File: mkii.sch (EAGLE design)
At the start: 52 parts, among them IC1 ATMEGA32U2, Q1 16MHz, U1 GTL2003, U2 TS1117, U3 PRTR5V0U2AX, X1 MINI-USB-32005-301

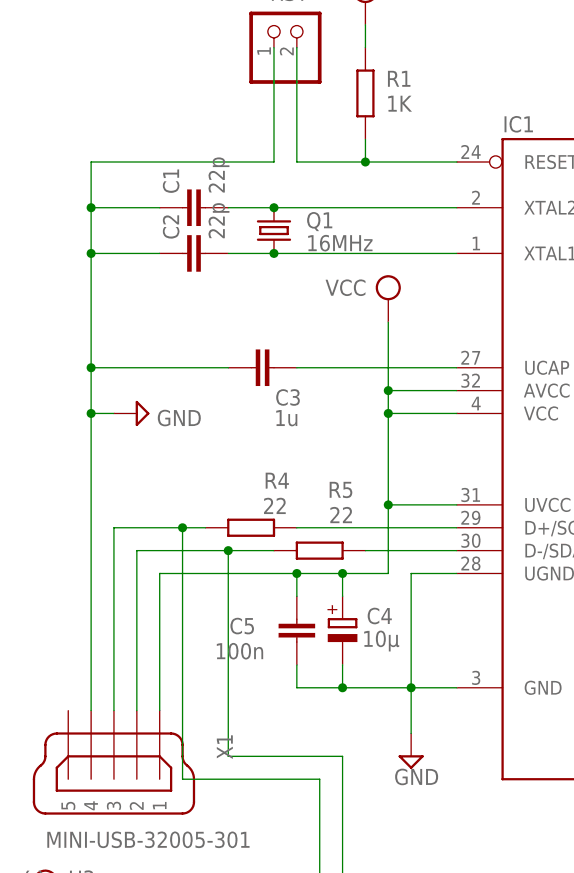
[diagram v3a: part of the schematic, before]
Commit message: pin4 on usb is id, pin5 is gnd. upstream idiots.
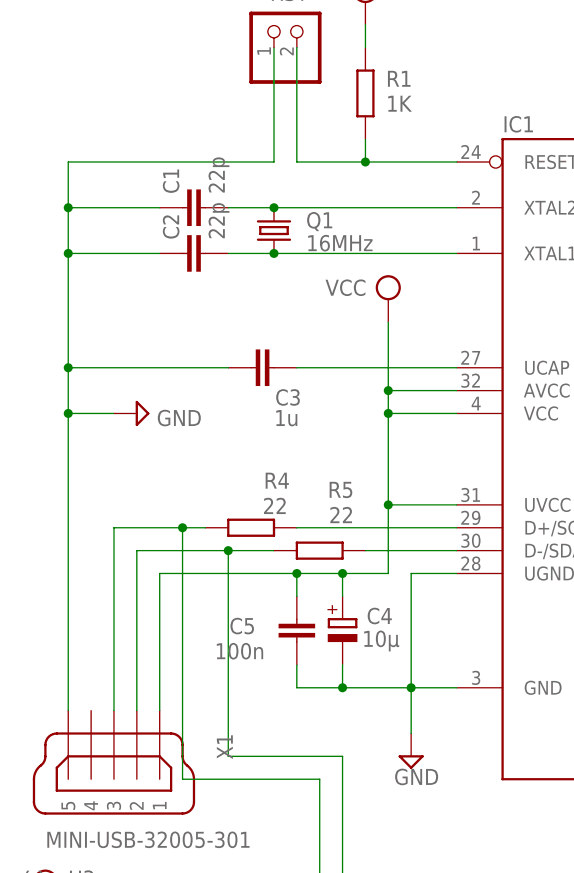
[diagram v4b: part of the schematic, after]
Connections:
- net GND: now also X1.5; no longer X1.4
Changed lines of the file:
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@@
 <net name="GND" class="1">
 <segment>
-<wire x1="20.32" y1="116.84" x2="12.7" y2="116.84" width="0.1524" layer="91"/>
-<wire x1="12.7" y1="116.84" x2="12.7" y2="111.76" width="0.1524" layer="91"/>
-<wire x1="20.32" y1="111.76" x2="12.7" y2="111.76" width="0.1524" layer="91"/>
-<wire x1="27.94" y1="99.06" x2="12.7" y2="99.06" width="0.1524" layer="91"/>
-<wire x1="12.7" y1="99.06" x2="12.7" y2="93.98" width="0.1524" layer="91"/>
-<wire x1="33.02" y1="121.92" x2="12.7" y2="121.92" width="0.1524" layer="91"/>
-<wire x1="12.7" y1="121.92" x2="12.7" y2="116.84" width="0.1524" layer="91"/>
-<wire x1="12.7" y1="60.96" x2="12.7" y2="93.98" width="0.1524" layer="91"/>
-<wire x1="12.7" y1="93.98" x2="15.24" y2="93.98" width="0.1524" layer="91"/>
-<wire x1="12.7" y1="111.76" x2="12.7" y2="99.06" width="0.1524" layer="91"/>
+<wire x1="20.32" y1="116.84" x2="10.16" y2="116.84" width="0.1524" layer="91"/>
+<wire x1="10.16" y1="116.84" x2="10.16" y2="111.76" width="0.1524" layer="91"/>
+<wire x1="20.32" y1="111.76" x2="10.16" y2="111.76" width="0.1524" layer="91"/>
+<wire x1="27.94" y1="99.06" x2="10.16" y2="99.06" width="0.1524" layer="91"/>
+<wire x1="10.16" y1="99.06" x2="10.16" y2="93.98" width="0.1524" layer="91"/>
+<wire x1="33.02" y1="121.92" x2="10.16" y2="121.92" width="0.1524" layer="91"/>
+<wire x1="10.16" y1="121.92" x2="10.16" y2="116.84" width="0.1524" layer="91"/>
+<wire x1="10.16" y1="93.98" x2="15.24" y2="93.98" width="0.1524" layer="91"/>
+<wire x1="10.16" y1="111.76" x2="10.16" y2="99.06" width="0.1524" layer="91"/>
 <wire x1="33.02" y1="121.92" x2="33.02" y2="134.62" width="0.1524" layer="91"/>
-<junction x="12.7" y="111.76"/>
-<junction x="12.7" y="116.84"/>
-<junction x="12.7" y="93.98"/>
-<junction x="12.7" y="99.06"/>
+<junction x="10.16" y="111.76"/>
+<junction x="10.16" y="116.84"/>
+<junction x="10.16" y="99.06"/>
 <pinref part="C1" gate="G$1" pin="1"/>
 <pinref part="C2" gate="G$1" pin="1"/>
@@
 <pinref part="RST" gate="A" pin="1"/>
 <pinref part="C3" gate="G$1" pin="1"/>
-<pinref part="X1" gate="G$1" pin="4"/>
+<pinref part="X1" gate="G$1" pin="5"/>
+<wire x1="10.16" y1="93.98" x2="10.16" y2="60.96" width="0.1524" layer="91"/>
+<junction x="10.16" y="93.98"/>
 </segment>
 <segment>

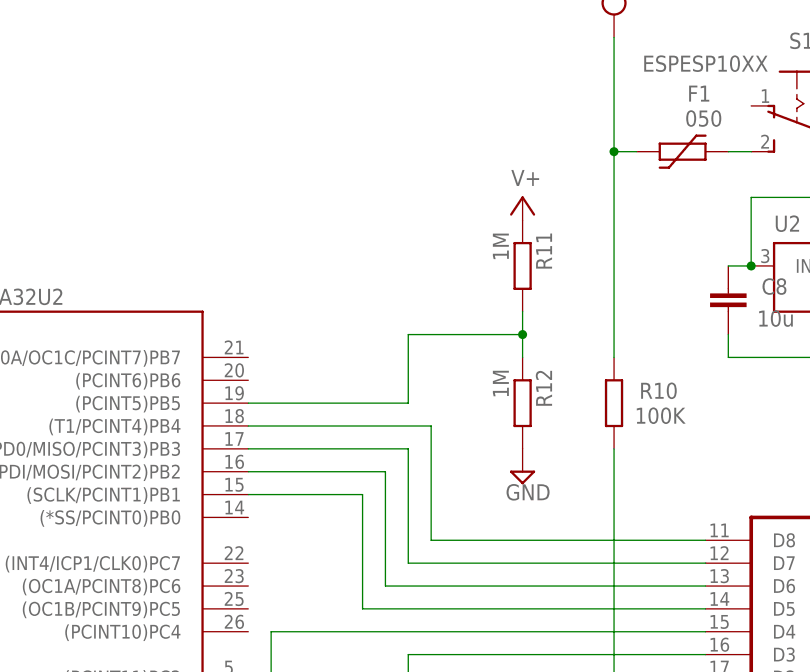
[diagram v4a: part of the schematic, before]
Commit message: remote circuit on pb5
can't remember my thoughts – without ADC there is no vbus
detection.
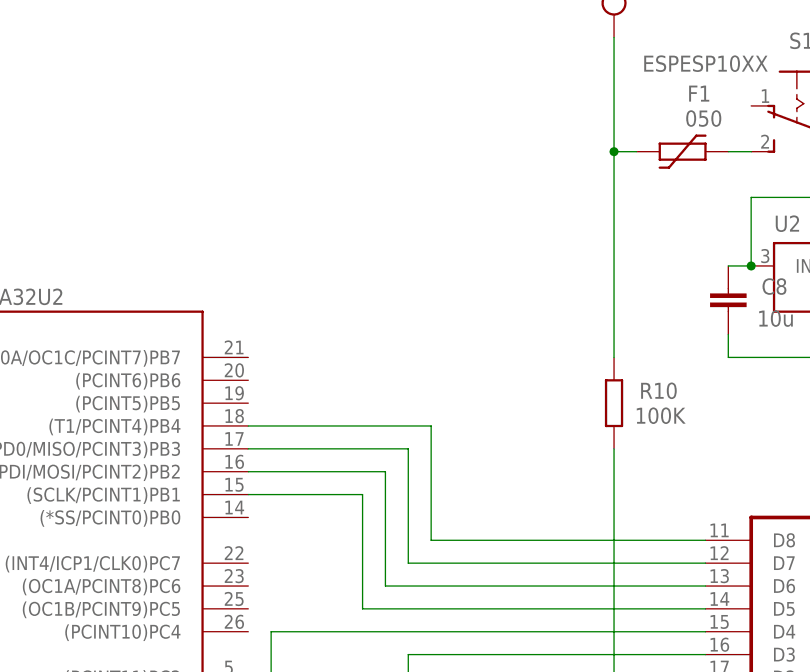
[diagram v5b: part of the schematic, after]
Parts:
- removed R11, R12: 1M, rcl:R-EU_R0603
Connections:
- removed net N$5: IC1.(PCINT5)PB5, R11.2, R12.1
- net GND: no longer R12.2
- net V+: no longer R11.1
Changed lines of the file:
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@@
 <part name="SV3" library="con-ml" deviceset="ML6" device="" value="TPI"/>
 <part name="FRAME1" library="frames" deviceset="A4L-LOC" device=""/>
-<part name="R11" library="rcl" deviceset="R-EU_" device="R0603" value="1M"/>
-<part name="R12" library="rcl" deviceset="R-EU_" device="R0603" value="1M"/>
-<part name="SUPPLY16" library="supply2" deviceset="GND" device=""/>
-<part name="SUPPLY17" library="supply2" deviceset="V+" device=""/>
 <part name="U$1" library="creative-commons" deviceset="CC" device="-TPLACE-HALF"/>
 <part name="U$2" library="creative-commons" deviceset="BY" device="-TPLACE-HS"/>
@@
 <instance part="SV3" gate="1" x="223.52" y="55.88" rot="R180"/>
 <instance part="FRAME1" gate="G$1" x="0" y="0"/>
-<instance part="R11" gate="G$1" x="134.62" y="129.54" rot="R270"/>
-<instance part="R12" gate="G$1" x="134.62" y="114.3" rot="R270"/>
-<instance part="SUPPLY16" gate="GND" x="134.62" y="106.68" smashed="yes">
-<attribute name="VALUE" x="132.715" y="103.505" size="1.778" layer="96"/>
-</instance>
-<instance part="SUPPLY17" gate="1" x="134.62" y="137.16" smashed="yes">
-<attribute name="VALUE" x="133.35" y="138.43" size="1.778" layer="96"/>
-</instance>
 <instance part="U$1" gate="G$1" x="215.9" y="20.32"/>
 <instance part="U$2" gate="G$1" x="220.98" y="20.32"/>
@@
 </segment>
 <segment>
-<pinref part="R12" gate="G$1" pin="2"/>
-<pinref part="SUPPLY16" gate="GND" pin="GND"/>
-</segment>
-<segment>
 <pinref part="U3" gate="G$1" pin="GND"/>
 <pinref part="SUPPLY18" gate="GND" pin="GND"/>
@@
 <wire x1="238.76" y1="86.36" x2="231.14" y2="86.36" width="0.1524" layer="91"/>
 </segment>
-<segment>
-<pinref part="R11" gate="G$1" pin="1"/>
-<pinref part="SUPPLY17" gate="1" pin="V+"/>
-</segment>
 </net>
 <net name="N$16" class="0">
@@
 </segment>
 </net>
-<net name="N$5" class="0">
-<segment>
-<pinref part="IC1" gate="AT90USB162" pin="(PCINT5)PB5"/>
-<wire x1="104.14" y1="114.3" x2="121.92" y2="114.3" width="0.1524" layer="91"/>
-<wire x1="121.92" y1="114.3" x2="121.92" y2="121.92" width="0.1524" layer="91"/>
-<wire x1="121.92" y1="121.92" x2="134.62" y2="121.92" width="0.1524" layer="91"/>
-<pinref part="R11" gate="G$1" pin="2"/>
-<wire x1="134.62" y1="121.92" x2="134.62" y2="124.46" width="0.1524" layer="91"/>
-<pinref part="R12" gate="G$1" pin="1"/>
-<wire x1="134.62" y1="119.38" x2="134.62" y2="121.92" width="0.1524" layer="91"/>
-<junction x="134.62" y="121.92"/>
-</segment>
-</net>

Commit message: unknown changes
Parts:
- C6, C8: device rcl:C-EUC0603 -> rcl:C-EUC0805
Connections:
- removed net N$23: C8.2, S1.P, S2.O, U2.IN
- new net N$2: S1.S, S2.P
- net N$6: now also C8.2, S2.O, U2.IN; no longer S1.S
- net V+: now also S1.P; no longer R7.2, S2.P
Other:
- moved on the sheet: S1, S2
